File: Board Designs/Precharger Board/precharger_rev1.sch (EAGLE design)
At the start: 23 parts, among them IC1 SN74AHC74, K1 RELAY

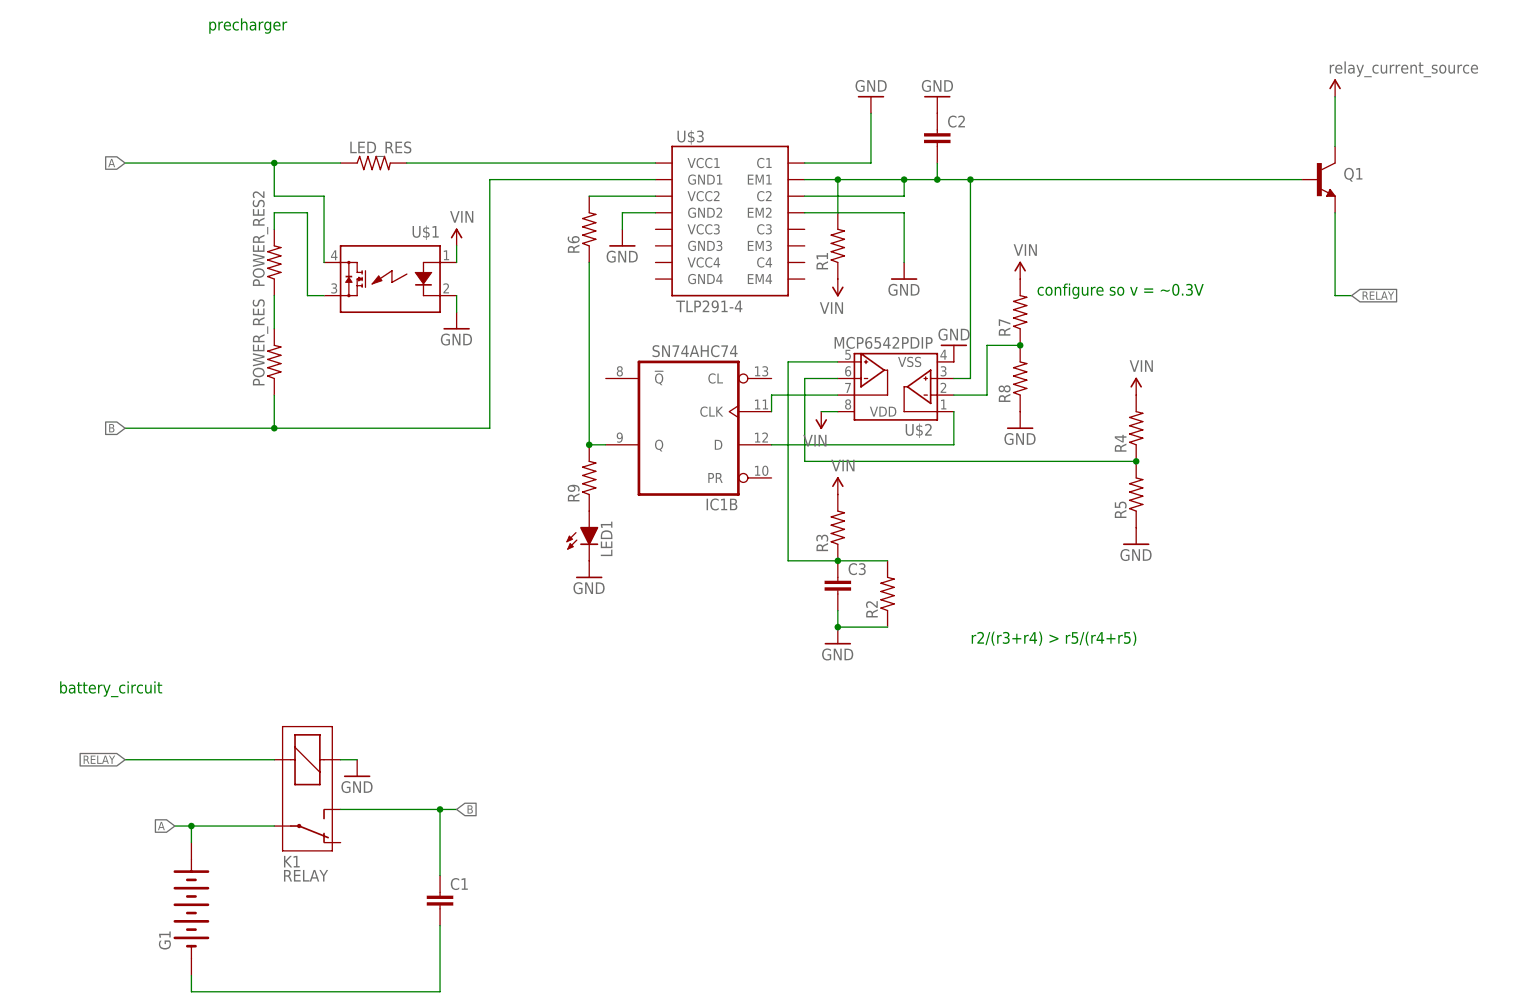
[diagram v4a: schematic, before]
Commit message: Created precharger board design
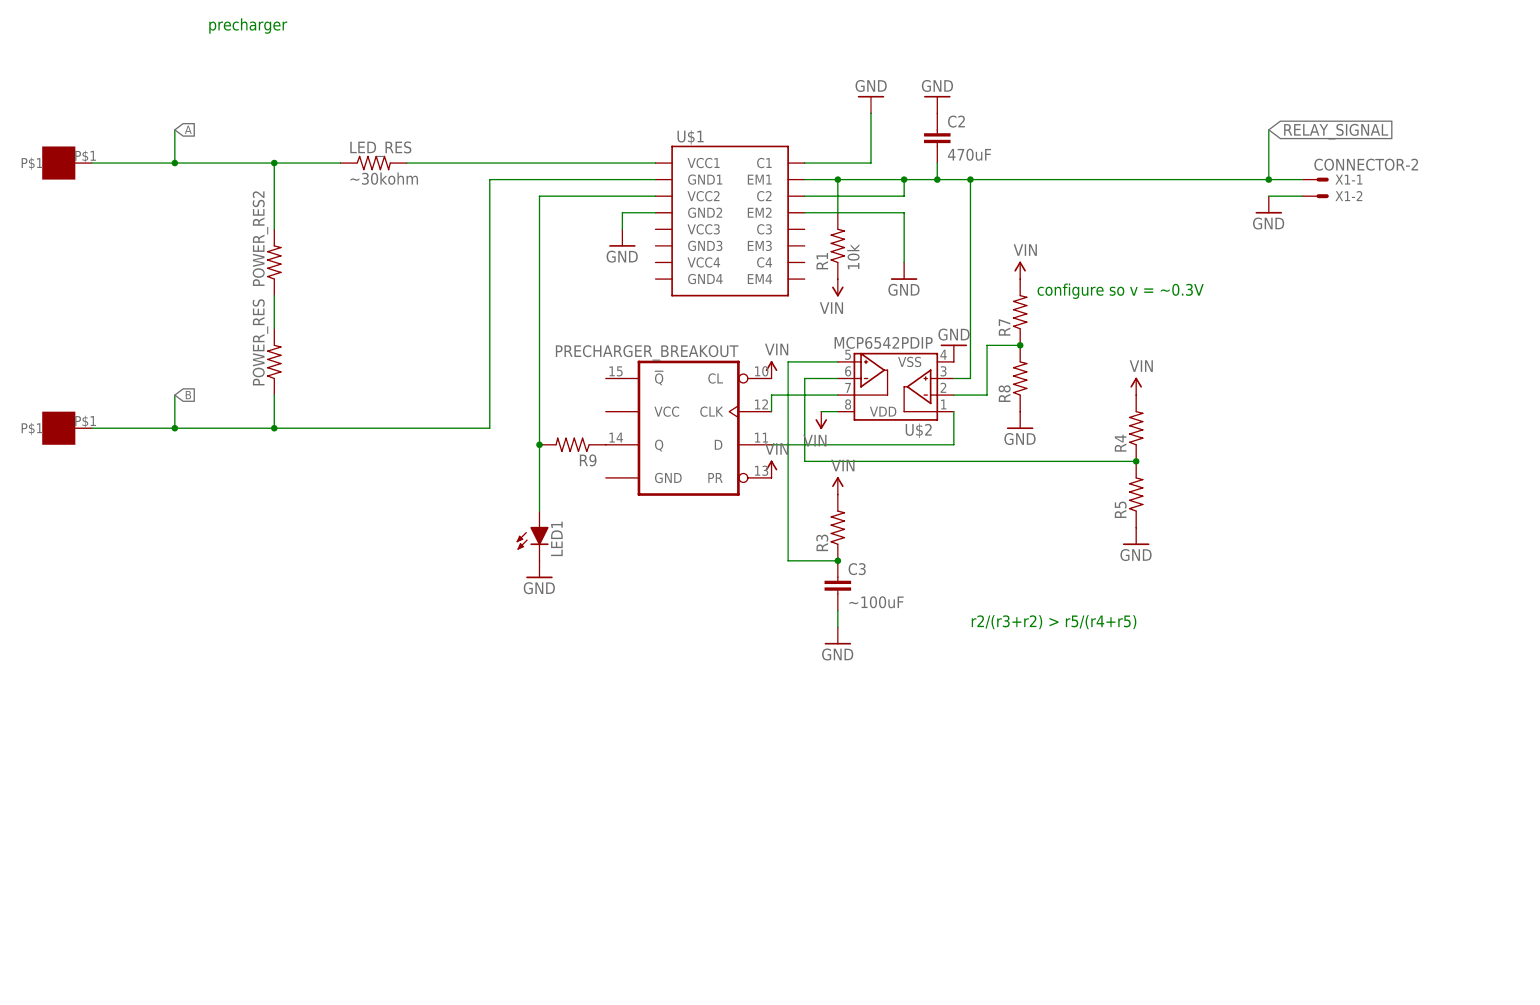
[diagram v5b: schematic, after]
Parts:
- removed C1: (no value), HyTechDevices:CAP0603-CAP
- removed G1: BATTERY_5_CELL, HyTechSymbols:BATTERY_5_CELL
- removed IC1: SN74AHC74, HyTechDevices:SN74AHC74
- removed K1: RELAY, HyTechSymbols:RELAY
- removed Q1: (no value), HyTechDevices:BJT_NPNTIP120
- removed R2, R6: (no value), HyTechDevices:RESISTOR0805-RES
- removed U$3: TLP291-4, HyTechDevices:TLP291-4
- added +, -: SOLDER_PAD, HyTechDevices:SOLDER_PAD
- added X1: CONNECTOR-2, HyTechDevices:CONNECTOR-2
- C2: value (none) -> 470uF; device HyTechDevices:CAP0603-CAP -> HyTechDevices:CAPPTH3
- C3: value (none) -> ~100uF; device HyTechDevices:CAP0805 -> HyTechDevices:CAPPTH1
- LED1: device HyTechDevices:LED-0805 -> HyTechDevices:LED-3MM
- LED_RES: value (none) -> ~30kohm; device HyTechDevices:RESISTOR0603 -> HyTechDevices:RESISTORAXIAL-0.3
- R1: value (none) -> 10k; device HyTechDevices:RESISTOR0603 -> HyTechDevices:RESISTORAXIAL-0.3
- R3, R4, R5, R7, R8, R9: device HyTechDevices:RESISTOR0805-RES -> HyTechDevices:RESISTORAXIAL-0.3
- U$1: value SOLID_STATE_RELAY_G3VM-41AY -> PRECHARGER_BREAKOUT; device HyTechDevices:SOLID_STATE_RELAY_G3VM-41AY -> HyTechDevices:PRECHARGER_BREAKOUT
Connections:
- removed net 12V: Q1.COLLECTOR
- removed net N$12: LED1.A, R9.1
- removed net N$3: C1.2, G1.-
- removed net N$9: R6.2
- removed net RELAY: C2.2, K1.2, Q1.BASE, Q1.EMITTER, R1.2, U$2.VINA+, U$3.C2, U$3.EM1
- new net RELAY_SIGNAL: C2.2, R1.2, U$1.C2, U$1.EM1, U$2.VINA+, X1-1.S
- net A: now also +.P$1, POWER_RES2.2; no longer G1.+, K1.P, U$1.IO1
- net B: now also -.P$1, U$1.GND1; no longer C1.1, K1.S, U$3.GND1
- net GND: now also U$1.C1, U$1.EM2, U$1.GND2, X1-2.S; no longer K1.1, R2.1, U$1.LED-, U$3.C1, U$3.EM2, U$3.GND2
- net N$1: now also R9.1, U$1.Q; no longer POWER_RES2.2, U$1.IO2
- net N$4: now also U$1.VCC1; no longer U$3.VCC1
- net N$5: now also U$1.CLK; no longer IC1B.CLK
- net N$6: now also U$1.D; no longer IC1B.D
- net N$7: now also LED1.A, U$1.VCC2; no longer IC1B.Q, R6.1
- net N$8: no longer R2.2
- net VIN: now also U$1.CL, U$1.PR; no longer U$1.LED+
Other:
- note added: "r2/(r3+r2) > r5/(r4+r5)"
- note removed: "battery_circuit"
- note removed: "r2/(r3+r4) > r5/(r4+r5)"
- moved on the sheet: LED1, R9

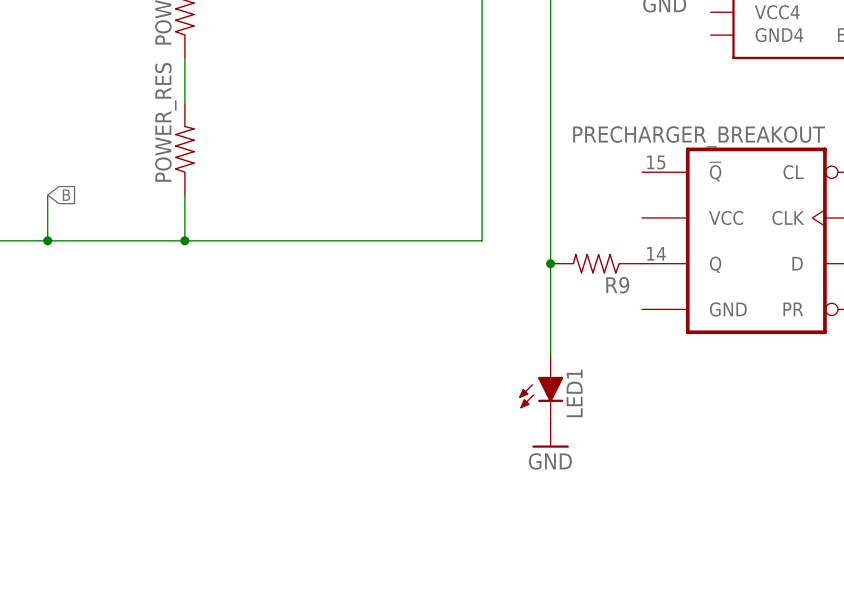
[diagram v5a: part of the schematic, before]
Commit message: Revised precharger prototype board design
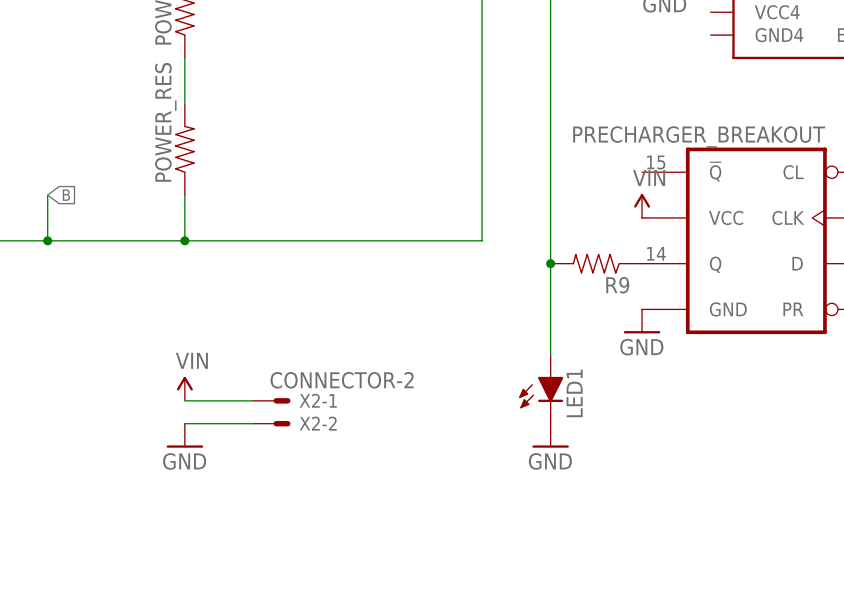
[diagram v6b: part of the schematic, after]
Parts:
- added X2: CONNECTOR-2, HyTechDevices:CONNECTOR-2
- C2: device HyTechDevices:CAPPTH3 -> HyTechDevices:CAPPTH1
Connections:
- net GND: now also U$1.GND, X2-2.S
- net VIN: now also U$1.VCC, X2-1.S
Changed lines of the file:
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@@
 <?xml version="1.0" encoding="utf-8"?>
 <!DOCTYPE eagle SYSTEM "eagle.dtd">
-<eagle version="8.3.2">
+<eagle version="8.6.0">
 <drawing>
 <settings>
@@
 <grid distance="0.1" unitdist="inch" unit="inch" style="lines" multiple="1" display="no" altdistance="0.01" altunitdist="inch" altunit="inch"/>
 <layers>
-<layer number="1" name="Top" color="4" fill="1" visible="no" active="no"/>
-<layer number="16" name="Bottom" color="1" fill="1" visible="no" active="no"/>
-<layer number="17" name="Pads" color="2" fill="1" visible="no" active="no"/>
-<layer number="18" name="Vias" color="2" fill="1" visible="no" active="no"/>
-<layer number="19" name="Unrouted" color="6" fill="1" visible="no" active="no"/>
-<layer number="20" name="Dimension" color="24" fill="1" visible="no" active="no"/>
-<layer number="21" name="tPlace" color="7" fill="1" visible="no" active="no"/>
-<layer number="22" name="bPlace" color="7" fill="1" visible="no" active="no"/>
-<layer number="23" name="tOrigins" color="15" fill="1" visible="no" active="no"/>
-<layer number="24" name="bOrigins" color="15" fill="1" visible="no" active="no"/>
-<layer number="25" name="tNames" color="7" fill="1" visible="no" active="no"/>
-<layer number="26" name="bNames" color="7" fill="1" visible="no" active="no"/>
-<layer number="27" name="tValues" color="7" fill="1" visible="no" active="no"/>
-<layer number="28" name="bValues" color="7" fill="1" visible="no" active="no"/>
+<layer number="1" name="Top" color="4" fill="1" visible="yes" active="no"/>
+<layer number="2" name="Route2" color="1" fill="3" visible="yes" active="no"/>
+<layer number="3" name="Route3" color="4" fill="3" visible="yes" active="no"/>
+<layer number="4" name="Route4" color="1" fill="4" visible="yes" active="no"/>
+<layer number="5" name="Route5" color="4" fill="4" visible="yes" active="no"/>
+<layer number="6" name="Route6" color="1" fill="8" visible="yes" active="no"/>
+<layer number="7" name="Route7" color="4" fill="8" visible="yes" active="no"/>
+<layer number="8" name="Route8" color="1" fill="2" visible="yes" active="no"/>
+<layer number="9" name="Route9" color="4" fill="2" visible="yes" active="no"/>
+<layer number="10" name="Route10" color="1" fill="7" visible="yes" active="no"/>
+<layer number="11" name="Route11" color="4" fill="7" visible="yes" active="no"/>
+<layer number="12" name="Route12" color="1" fill="5" visible="yes" active="no"/>
+<layer number="13" name="Route13" color="4" fill="5" visible="yes" active="no"/>
+<layer number="14" name="Route14" color="1" fill="6" visible="yes" active="no"/>
+<layer number="15" name="Route15" color="4" fill="6" visible="yes" active="no"/>
+<layer number="16" name="Bottom" color="1" fill="1" visible="yes" active="no"/>
+<layer number="17" name="Pads" color="2" fill="1" visible="yes" active="no"/>
+<layer number="18" name="Vias" color="2" fill="1" visible="yes" active="no"/>
+<layer number="19" name="Unrouted" color="6" fill="1" visible="yes" active="no"/>
+<layer number="20" name="Dimension" color="24" fill="1" visible="yes" active="no"/>
+<layer number="21" name="tPlace" color="7" fill="1" visible="yes" active="no"/>
+<layer number="22" name="bPlace" color="7" fill="1" visible="yes" active="no"/>
+<layer number="23" name="tOrigins" color="15" fill="1" visible="yes" active="no"/>
+<layer number="24" name="bOrigins" color="15" fill="1" visible="yes" active="no"/>
+<layer number="25" name="tNames" color="7" fill="1" visible="yes" active="no"/>
+<layer number="26" name="bNames" color="7" fill="1" visible="yes" active="no"/>
+<layer number="27" name="tValues" color="7" fill="1" visible="yes" active="no"/>
+<layer number="28" name="bValues" color="7" fill="1" visible="yes" active="no"/>
 <layer number="29" name="tStop" color="7" fill="3" visible="no" active="no"/>
 <layer number="30" name="bStop" color="7" fill="6" visible="no" active="no"/>
@@
 <layer number="35" name="tGlue" color="7" fill="4" visible="no" active="no"/>
 <layer number="36" name="bGlue" color="7" fill="5" visible="no" active="no"/>
-<layer number="37" name="tTest" color="7" fill="1" visible="no" active="no"/>
-<layer number="38" name="bTest" color="7" fill="1" visible="no" active="no"/>
+<layer number="37" name="tTest" color="7" fill="1" visible="yes" active="no"/>
+<layer number="38" name="bTest" color="7" fill="1" visible="yes" active="no"/>
 <layer number="39" name="tKeepout" color="4" fill="11" visible="no" active="no"/>
 <layer number="40" name="bKeepout" color="1" fill="11" visible="no" active="no"/>
@@
 <layer number="44" name="Drills" color="7" fill="1" visible="no" active="no"/>
 <layer number="45" name="Holes" color="7" fill="1" visible="no" active="no"/>
-<layer number="46" name="Milling" color="3" fill="1" visible="no" active="no"/>
-<layer number="47" name="Measures" color="7" fill="1" visible="no" active="no"/>
-<layer number="48" name="Document" color="7" fill="1" visible="no" active="no"/>
-<layer number="49" name="Reference" color="7" fill="1" visible="no" active="no"/>
-<layer number="50" name="dxf" color="7" fill="1" visible="no" active="no"/>
-<layer number="51" name="tDocu" color="7" fill="1" visible="no" active="no"/>
-<layer number="52" name="bDocu" color="7" fill="1" visible="no" active="no"/>
-<layer number="53" name="tGND_GNDA" color="7" fill="9" visible="no" active="no"/>
-<layer number="54" name="bGND_GNDA" color="1" fill="9" visible="no" active="no"/>
-<layer number="56" name="wert" color="7" fill="1" visible="no" active="no"/>
-<layer number="57" name="tCAD" color="7" fill="1" visible="no" active="no"/>
-<layer number="59" name="tCarbon" color="7" fill="1" visible="no" active="no"/>
-<layer number="60" name="bCarbon" color="7" fill="1" visible="no" active="no"/>
+<layer number="46" name="Milling" color="3" fill="1" visible="yes" active="no"/>
+<layer number="47" name="Measures" color="7" fill="1" visible="yes" active="no"/>
+<layer number="48" name="Document" color="7" fill="1" visible="yes" active="no"/>
+<layer number="49" name="Reference" color="7" fill="1" visible="yes" active="no"/>
+<layer number="50" name="dxf" color="7" fill="1" visible="yes" active="no"/>
+<layer number="51" name="tDocu" color="7" fill="1" visible="yes" active="no"/>
+<layer number="52" name="bDocu" color="7" fill="1" visible="yes" active="no"/>
+<layer number="53" name="tGND_GNDA" color="7" fill="9" visible="yes" active="no"/>
+<layer number="54" name="bGND_GNDA" color="1" fill="9" visible="yes" active="no"/>
+<layer number="56" name="wert" color="7" fill="1" visible="yes" active="no"/>
+<layer number="57" name="tCAD" color="7" fill="1" visible="yes" active="no"/>
+<layer number="59" name="tCarbon" color="7" fill="1" visible="yes" active="no"/>
+<layer number="60" name="bCarbon" color="7" fill="1" visible="yes" active="no"/>
 <layer number="88" name="SimResults" color="9" fill="1" visible="yes" active="yes"/>
 <layer number="89" name="SimProbes" color="9" fill="1" visible="yes" active="yes"/>
@@
 <part name="LED_RES" library="HyTechDevices" deviceset="RESISTOR" device="AXIAL-0.3" value="~30kohm"/>
 <part name="R1" library="HyTechDevices" deviceset="RESISTOR" device="AXIAL-0.3" value="10k"/>
-<part name="C2" library="HyTechDevices" deviceset="CAP" device="PTH3" value="470uF"/>
+<part name="C2" library="HyTechDevices" deviceset="CAP" device="PTH1" value="470uF"/>
 <part name="GND1" library="HyTechSymbols" deviceset="GND" device=""/>
 <part name="GND2" library="HyTechSymbols" deviceset="GND" device=""/>
@@
 <part name="X1" library="HyTechDevices" deviceset="CONNECTOR-2" device=""/>
 <part name="GND3" library="HyTechSymbols" deviceset="GND" device=""/>
+<part name="SUPPLY8" library="HyTechSymbols" deviceset="VIN" device=""/>
+<part name="GND11" library="HyTechSymbols" deviceset="GND" device=""/>
+<part name="GND12" library="HyTechSymbols" deviceset="GND" device=""/>
+<part name="SUPPLY9" library="HyTechSymbols" deviceset="VIN" device=""/>
+<part name="X2" library="HyTechDevices" deviceset="CONNECTOR-2" device=""/>
 </parts>
 <sheets>
@@
 <instance part="X1" gate="-1" x="256.54" y="76.2"/>
 <instance part="GND3" gate="1" x="248.92" y="71.12"/>
+<instance part="SUPPLY8" gate="G$1" x="147.32" y="40.64"/>
+<instance part="GND11" gate="1" x="147.32" y="27.94"/>
+<instance part="GND12" gate="1" x="96.52" y="15.24"/>
+<instance part="SUPPLY9" gate="G$1" x="96.52" y="20.32"/>
+<instance part="X2" gate="-2" x="106.68" y="17.78"/>
+<instance part="X2" gate="-1" x="106.68" y="20.32"/>
 </instances>
 <busses>
@@
 <wire x1="254" y1="73.66" x2="248.92" y2="73.66" width="0.1524" layer="91"/>
 <pinref part="GND3" gate="1" pin="GND"/>
+</segment>
+<segment>
+<pinref part="U$1" gate="G$1" pin="GND"/>
+<pinref part="GND11" gate="1" pin="GND"/>
+</segment>
+<segment>
+<pinref part="X2" gate="-2" pin="S"/>
+<pinref part="GND12" gate="1" pin="GND"/>
+<wire x1="104.14" y1="17.78" x2="96.52" y2="17.78" width="0.1524" layer="91"/>
 </segment>
 </net>
@@
 <pinref part="U$1" gate="G$1" pin="PR"/>
 </segment>
-</net>
+<segment>
+<pinref part="U$1" gate="G$1" pin="VCC"/>
+<pinref part="SUPPLY8" gate="G$1" pin="VIN"/>
+</segment>
+<segment>
+<pinref part="SUPPLY9" gate="G$1" pin="VIN"/>
+<pinref part="X2" gate="-1" pin="S"/>
+<wire x1="96.52" y1="20.32" x2="104.14" y2="20.32" width="0.1524" layer="91"/>
+</segment>
+</net>
